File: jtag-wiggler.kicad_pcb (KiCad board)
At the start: 2 copper layers, 152.4 x 101.6 mm, 50 parts, among them J1 DSUB-25_Male_Horizontal_P2.77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, J2 BarrelJack_Horizontal, P1 PinHeader_1x02_P2.54mm_Vertic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, P2 PinHeader_1x03_P2.54mm_Vertic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, P3 PinHeader_1x08_P2.54mm_Vertic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, Q1 TO-92_Wide, SW1 SW_Generic, U1 DIP-20_W7.62mm_Socket_LongPads, U2 TO-220-3_Vertical, U3 TO-220-3_Vertical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

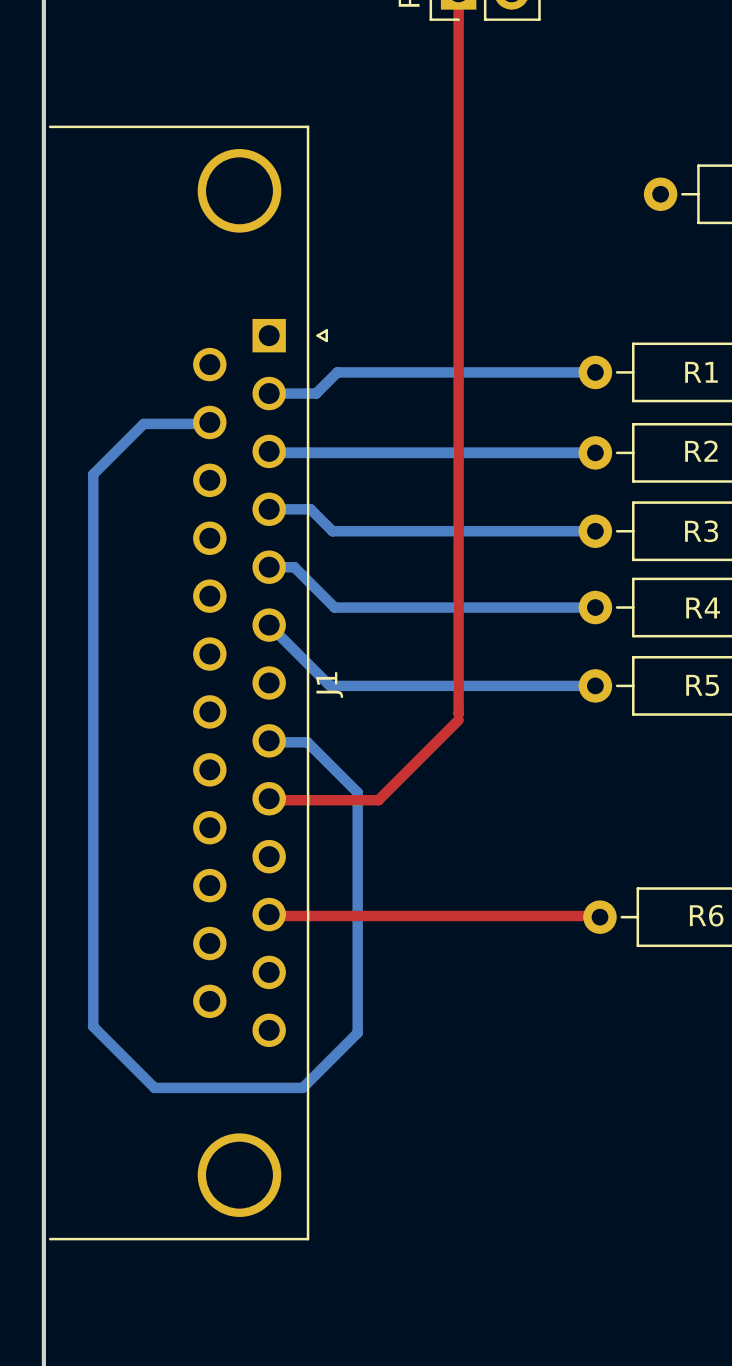
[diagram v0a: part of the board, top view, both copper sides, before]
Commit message: Remove extra track from D2; general PCB cleanup
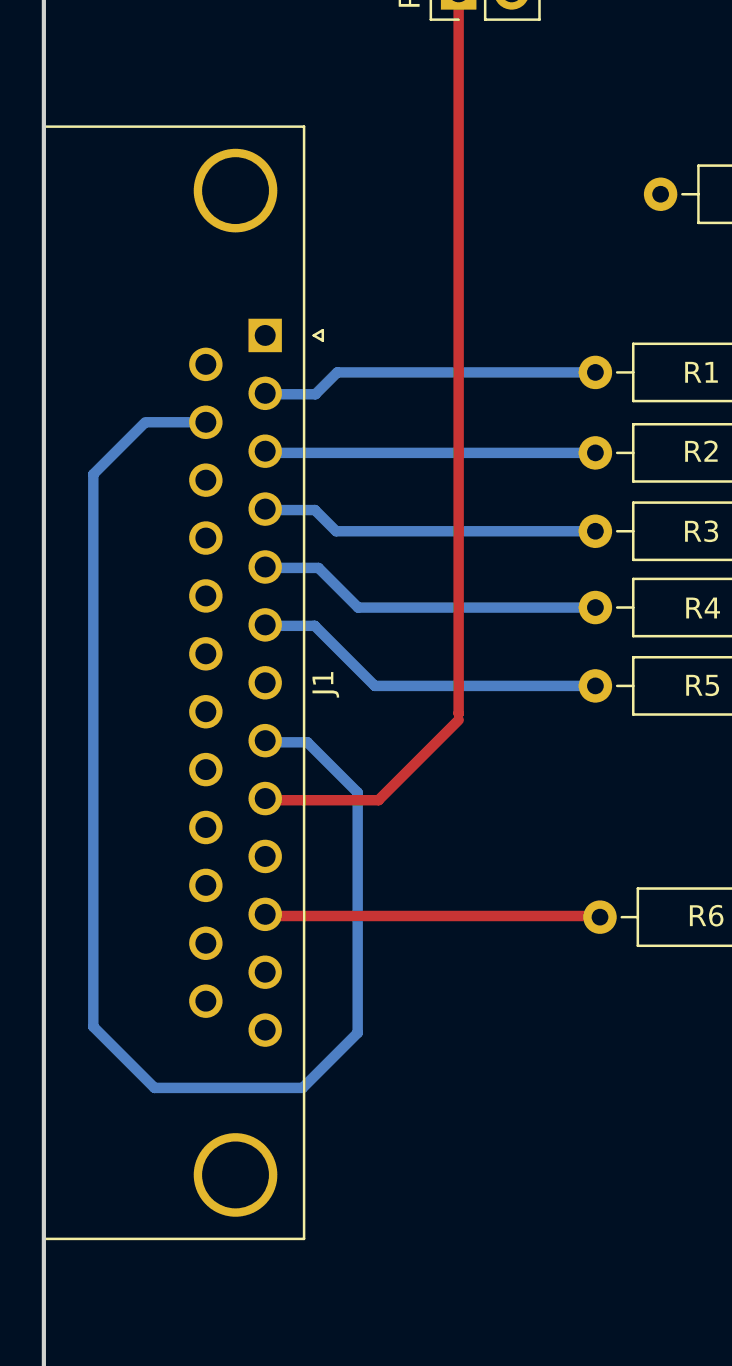
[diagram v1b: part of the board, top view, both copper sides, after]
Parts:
- moved J1 0.19 mm to (84.2, 82.2)
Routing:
- net D2: track 31.8 -> 15.7 mm
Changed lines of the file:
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@@
   )
   (footprint "Connector_Dsub:DSUB-25_Male_Horizontal_P2.77x2.84mm_EdgePinOffset7.70mm_Housed_MountingHolesOffset9.12mm" (layer "F.Cu")
-    (at 84.44 82.19 -90)
+    (at 84.25 82.18 -90)
     (descr "25-pin D-Sub connector, horizontal/angled (90 deg), THT-mount, male, pitch 2.77x2.84mm, pin-PCB-offset 7.699999999999999mm, distance of mounting holes 47.1mm, distance of mounting holes to PCB edge 9.12mm, see https://disti-assets.s3.amazonaws.com/tonar/files/datasheets/16730.pdf")
     (tags "25-pin D-Sub connector horizontal angled 90deg THT male pitch 2.77x2.84mm pin-PCB-offset 7.699999999999999mm mounting-holes-distance 47.1mm mounting-hole-offset 47.1mm")
@@
   (segment (start 174.85 127.925) (end 174.8 127.875) (width 0.5) (layer "F.Cu") (net 2))
   (segment (start 174.85 135.475) (end 174.85 127.925) (width 0.75) (layer "F.Cu") (net 2))
-  (segment (start 86.69 84.96) (end 84.44 84.96) (width 0.5) (layer "B.Cu") (net 4))
-  (segment (start 87.7 83.95) (end 86.69 84.96) (width 0.5) (layer "B.Cu") (net 4))
+  (segment (start 84.425 84.995) (end 86.655 84.995) (width 0.5) (layer "B.Cu") (net 4))
+  (segment (start 86.655 84.995) (end 87.7 83.95) (width 0.5) (layer "B.Cu") (net 4))
   (segment (start 87.7 83.95) (end 100.05 83.95) (width 0.5) (layer "B.Cu") (net 4))
   (segment (start 119.87 69.395) (end 119.825 69.35) (width 0.5) (layer "F.Cu") (net 5))
@@
   (segment (start 211.790056 99.855) (end 205.850056 99.855) (width 0.5) (layer "F.Cu") (net 8))
   (segment (start 211.490056 106.709944) (end 212.7 107.919888) (width 0.5) (layer "F.Cu") (net 8))
-  (segment (start 84.315 87.8) (end 100.345 87.8) (width 0.5) (layer "B.Cu") (net 9))
   (segment (start 84.315 87.8) (end 100.05 87.8) (width 0.5) (layer "B.Cu") (net 9))
   (segment (start 194.8 88.6) (end 188.65 82.45) (width 0.5) (layer "F.Cu") (net 10))
@@
   (segment (start 100.215 109.96) (end 100.27 110.015) (width 0.5) (layer "F.Cu") (net 20))
   (segment (start 84.315 109.96) (end 100.215 109.96) (width 0.5) (layer "F.Cu") (net 20))
-  (segment (start 87.475 98.95) (end 100.05 98.95) (width 0.5) (layer "B.Cu") (net 21))
-  (segment (start 84.44 96.04) (end 87.35 98.95) (width 0.5) (layer "B.Cu") (net 21))
-  (segment (start 87.35 98.95) (end 87.475 98.95) (width 0.25) (layer "B.Cu") (net 21))
-  (segment (start 85.645 93.27) (end 87.575 95.2) (width 0.5) (layer "B.Cu") (net 22))
-  (segment (start 100.05 95.2) (end 87.575 95.2) (width 0.5) (layer "B.Cu") (net 22))
-  (segment (start 84.44 93.27) (end 85.645 93.27) (width 0.5) (layer "B.Cu") (net 22))
-  (segment (start 100.05 91.55) (end 87.475 91.55) (width 0.5) (layer "B.Cu") (net 23))
-  (segment (start 87.475 91.55) (end 86.425 90.5) (width 0.5) (layer "B.Cu") (net 23))
-  (segment (start 86.425 90.5) (end 84.44 90.5) (width 0.5) (layer "B.Cu") (net 23))
+  (segment (start 86.62 96.075) (end 89.495 98.95) (width 0.5) (layer "B.Cu") (net 21))
+  (segment (start 89.495 98.95) (end 100.05 98.95) (width 0.5) (layer "B.Cu") (net 21))
+  (segment (start 84.425 96.075) (end 86.62 96.075) (width 0.5) (layer "B.Cu") (net 21))
+  (segment (start 84.425 93.305) (end 86.8 93.305) (width 0.5) (layer "B.Cu") (net 22))
+  (segment (start 88.695 95.2) (end 100.05 95.2) (width 0.5) (layer "B.Cu") (net 22))
+  (segment (start 86.8 93.305) (end 88.695 95.2) (width 0.5) (layer "B.Cu") (net 22))
+  (segment (start 87.645 91.55) (end 100.05 91.55) (width 0.5) (layer "B.Cu") (net 23))
+  (segment (start 86.63 90.535) (end 87.645 91.55) (width 0.5) (layer "B.Cu") (net 23))
+  (segment (start 84.425 90.535) (end 86.63 90.535) (width 0.5) (layer "B.Cu") (net 23))
   (segment (start 214.140056 83.044944) (end 214.065 83.12) (width 0.5) (layer "F.Cu") (net 24))
   (segment (start 198.693 60.99) (end 198.693 67.118) (width 0.5) (layer "F.Cu") (net 24))
@@
   (segment (start 93.51 100.275) (end 93.505 100.27) (width 0.5) (layer "F.Cu") (net 33))
   (segment (start 76.025 115.2545) (end 78.9567 118.1862) (width 0.5) (layer "B.Cu") (net 34))
-  (segment (start 81.475 86.415) (end 78.435 86.415) (width 0.5) (layer "B.Cu") (net 34))
   (segment (start 88.675 104.055) (end 86.27 101.65) (width 0.5) (layer "B.Cu") (net 34))
   (segment (start 88.675 115.5529) (end 88.675 104.055) (width 0.5) (layer "B.Cu") (net 34))
@@
   (segment (start 76.025 88.825) (end 76.025 115.2545) (width 0.5) (layer "B.Cu") (net 34))
   (segment (start 78.435 86.415) (end 76.025 88.825) (width 0.5) (layer "B.Cu") (net 34))
+  (segment (start 81.41 86.335) (end 78.515 86.335) (width 0.5) (layer "B.Cu") (net 34))
   (segment (start 78.9567 118.1862) (end 86.0417 118.1862) (width 0.5) (layer "B.Cu") (net 34))
   (segment (start 135.63 98.325) (end 135.63 102.355) (width 0.5) (layer "F.Cu") (net 35))
